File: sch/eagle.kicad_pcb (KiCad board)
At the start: 2 copper layers, 0 parts

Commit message: Added pcb outline
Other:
- board outline added: 46 x 68 mm
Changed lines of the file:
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@@
 	)
 	(net 0 "")
+	(gr_arc
+		(start 130 134)
+		(mid 127.87868 133.12132)
+		(end 127 131)
+		(stroke
+			(width 0.05)
+			(type default)
+		)
+		(layer "Edge.Cuts")
+	)
+	(gr_arc
+		(start 170 66)
+		(mid 172.12132 66.87868)
+		(end 173 69)
+		(stroke
+			(width 0.05)
+			(type default)
+		)
+		(layer "Edge.Cuts")
+	)
+	(gr_arc
+		(start 173 131)
+		(mid 172.12132 133.12132)
+		(end 170 134)
+		(stroke
+			(width 0.05)
+			(type default)
+		)
+		(layer "Edge.Cuts")
+	)
+	(gr_line
+		(start 127 69)
+		(end 127 131)
+		(stroke
+			(width 0.05)
+			(type default)
+		)
+		(layer "Edge.Cuts")
+	)
+	(gr_line
+		(start 130 66)
+		(end 170 66)
+		(stroke
+			(width 0.05)
+			(type default)
+		)
+		(layer "Edge.Cuts")
+	)
+	(gr_circle
+		(center 170 69)
+		(end 171.6 69)
+		(stroke
+			(width 0.05)
+			(type default)
+		)
+		(fill none)
+		(layer "Edge.Cuts")
+	)
+	(gr_circle
+		(center 130 131)
+		(end 131.6 131)
+		(stroke
+			(width 0.05)
+			(type default)
+		)
+		(fill none)
+		(layer "Edge.Cuts")
+	)
+	(gr_circle
+		(center 170 131)
+		(end 171.6 131)
+		(stroke
+			(width 0.05)
+			(type default)
+		)
+		(fill none)
+		(layer "Edge.Cuts")
+	)
+	(gr_line
+		(start 173 69)
+		(end 173 131)
+		(stroke
+			(width 0.05)
+			(type default)
+		)
+		(layer "Edge.Cuts")
+	)
+	(gr_line
+		(start 170 134)
+		(end 130 134)
+		(stroke
+			(width 0.05)
+			(type default)
+		)
+		(layer "Edge.Cuts")
+	)
+	(gr_arc
+		(start 127 69)
+		(mid 127.87868 66.87868)
+		(end 130 66)
+		(stroke
+			(width 0.05)
+			(type default)
+		)
+		(layer "Edge.Cuts")
+	)
+	(gr_circle
+		(center 130 69)
+		(end 131.6 69)
+		(stroke
+			(width 0.05)
+			(type default)
+		)
+		(fill none)
+		(layer "Edge.Cuts")
+	)
 )

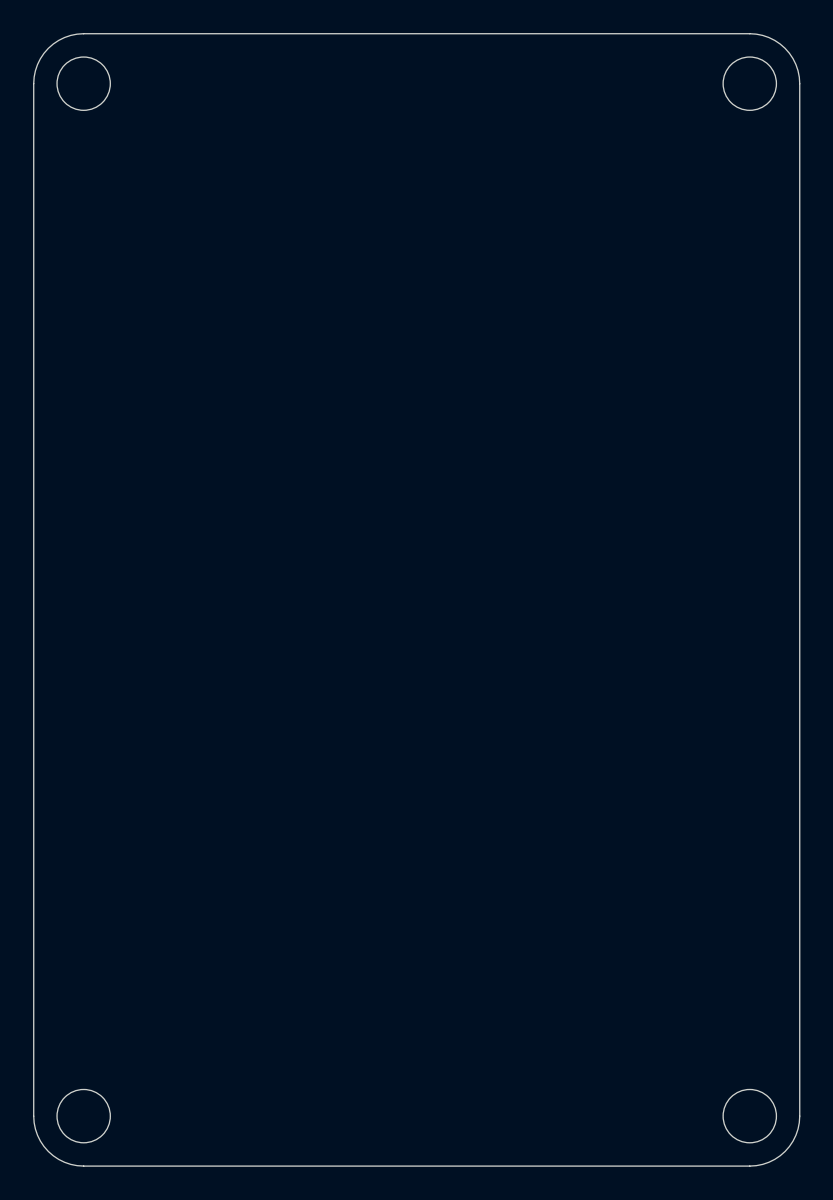
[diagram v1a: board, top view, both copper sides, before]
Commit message: Changed board size
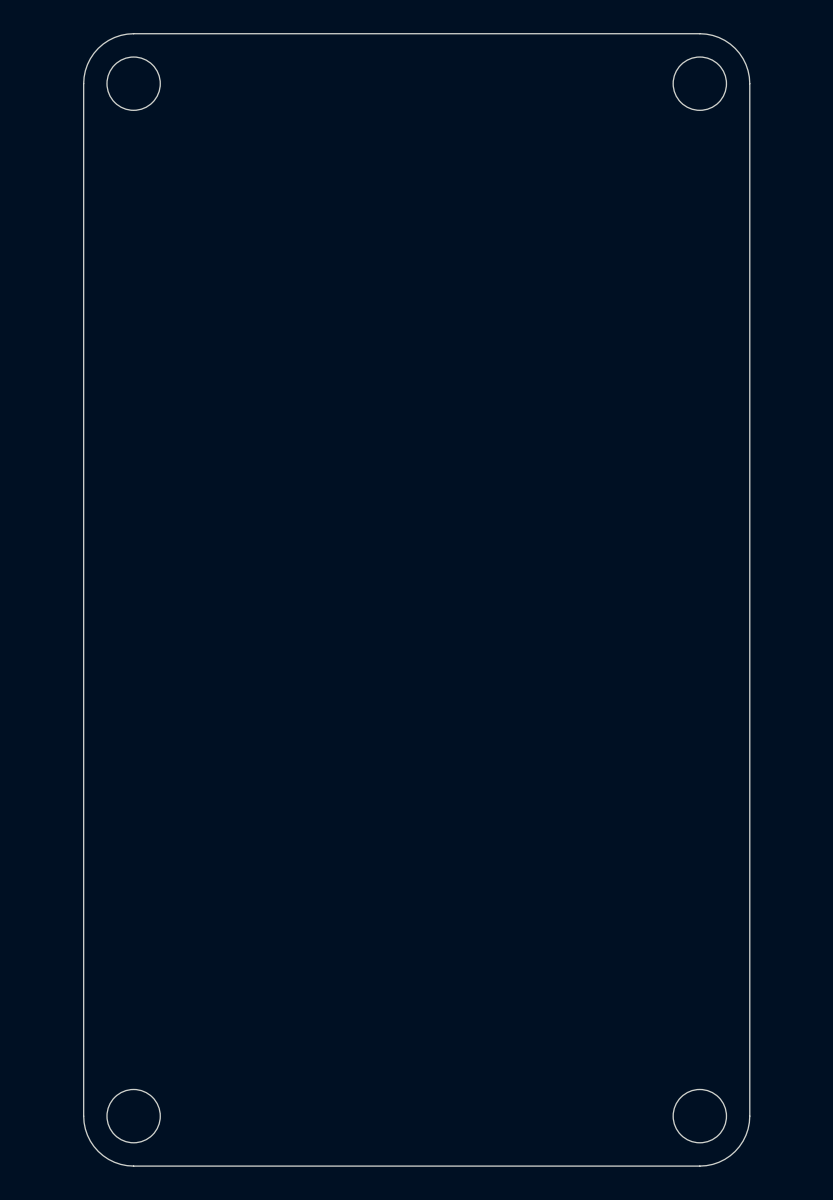
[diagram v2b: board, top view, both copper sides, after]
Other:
- board size 46 x 68 mm -> 40 x 68 mm
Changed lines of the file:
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@@
 	(net 0 "")
 	(gr_arc
-		(start 130 134)
-		(mid 127.87868 133.12132)
-		(end 127 131)
+		(start 133 134)
+		(mid 130.87868 133.12132)
+		(end 130 131)
 		(stroke
 			(width 0.05)
@@
 	)
 	(gr_arc
-		(start 170 66)
-		(mid 172.12132 66.87868)
-		(end 173 69)
+		(start 167 66)
+		(mid 169.12132 66.87868)
+		(end 170 69)
 		(stroke
 			(width 0.05)
@@
 	)
 	(gr_arc
-		(start 173 131)
-		(mid 172.12132 133.12132)
-		(end 170 134)
+		(start 170 131)
+		(mid 169.12132 133.12132)
+		(end 167 134)
 		(stroke
 			(width 0.05)
@@
 	)
 	(gr_line
-		(start 127 69)
-		(end 127 131)
+		(start 130 69)
+		(end 130 131)
 		(stroke
 			(width 0.05)
@@
 	)
 	(gr_line
-		(start 130 66)
-		(end 170 66)
+		(start 133 66)
+		(end 167 66)
 		(stroke
 			(width 0.05)
@@
 	)
 	(gr_circle
-		(center 170 69)
-		(end 171.6 69)
+		(center 167 69)
+		(end 168.6 69)
 		(stroke
 			(width 0.05)
@@
 	)
 	(gr_circle
-		(center 130 131)
-		(end 131.6 131)
+		(center 133 131)
+		(end 134.6 131)
 		(stroke
 			(width 0.05)
@@
 	)
 	(gr_circle
-		(center 170 131)
-		(end 171.6 131)
+		(center 167 131)
+		(end 168.6 131)
 		(stroke
 			(width 0.05)
@@
 	)
 	(gr_line
-		(start 173 69)
-		(end 173 131)
+		(start 170 69)
+		(end 170 131)
 		(stroke
 			(width 0.05)
@@
 	)
 	(gr_line
-		(start 170 134)
-		(end 130 134)
+		(start 167 134)
+		(end 133 134)
 		(stroke
 			(width 0.05)
@@
 	)
 	(gr_arc
-		(start 127 69)
-		(mid 127.87868 66.87868)
-		(end 130 66)
+		(start 130 69)
+		(mid 130.87868 66.87868)
+		(end 133 66)
 		(stroke
 			(width 0.05)
@@
 	)
 	(gr_circle
-		(center 130 69)
-		(end 131.6 69)
+		(center 133 69)
+		(end 134.6 69)
 		(stroke
 			(width 0.05)
